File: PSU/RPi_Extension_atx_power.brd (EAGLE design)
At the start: 63 x 50 mm, 8 parts, among them J1 ATX24RH, J2 J2

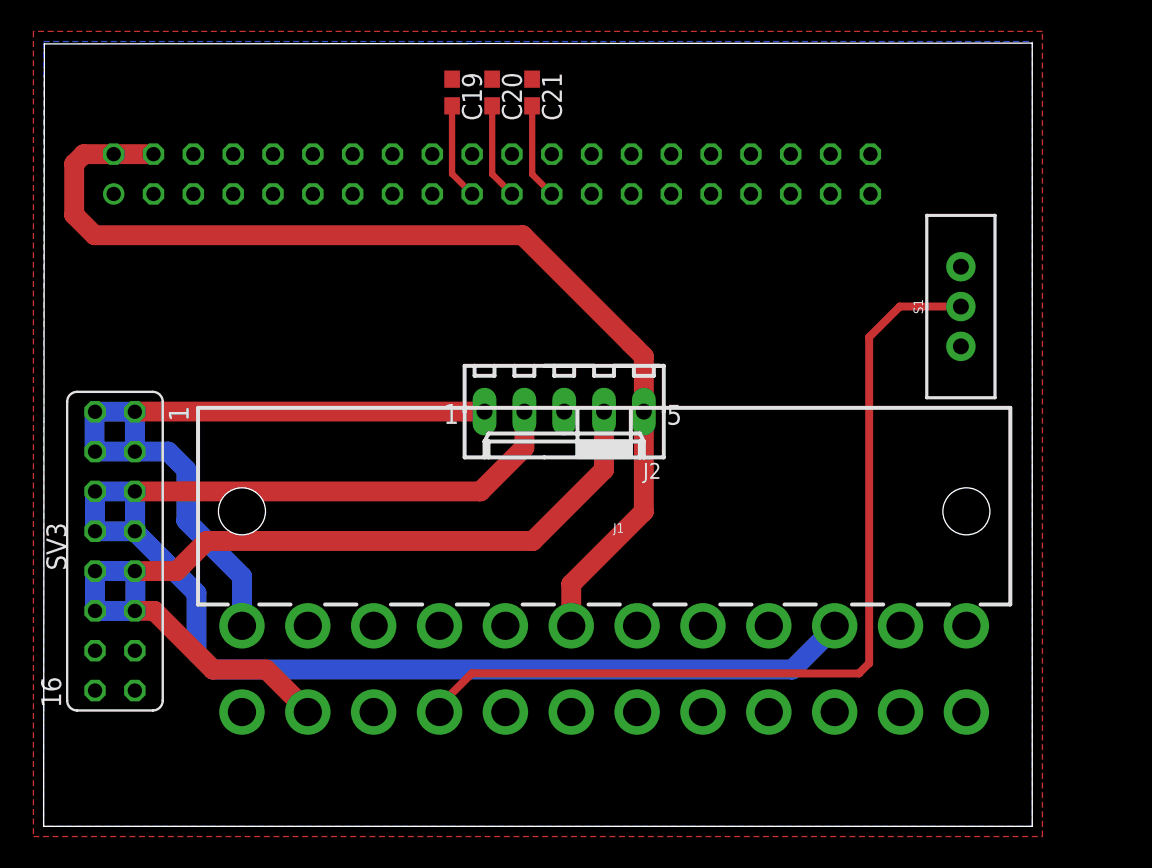
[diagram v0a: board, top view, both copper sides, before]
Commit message: added vertical connector to power board
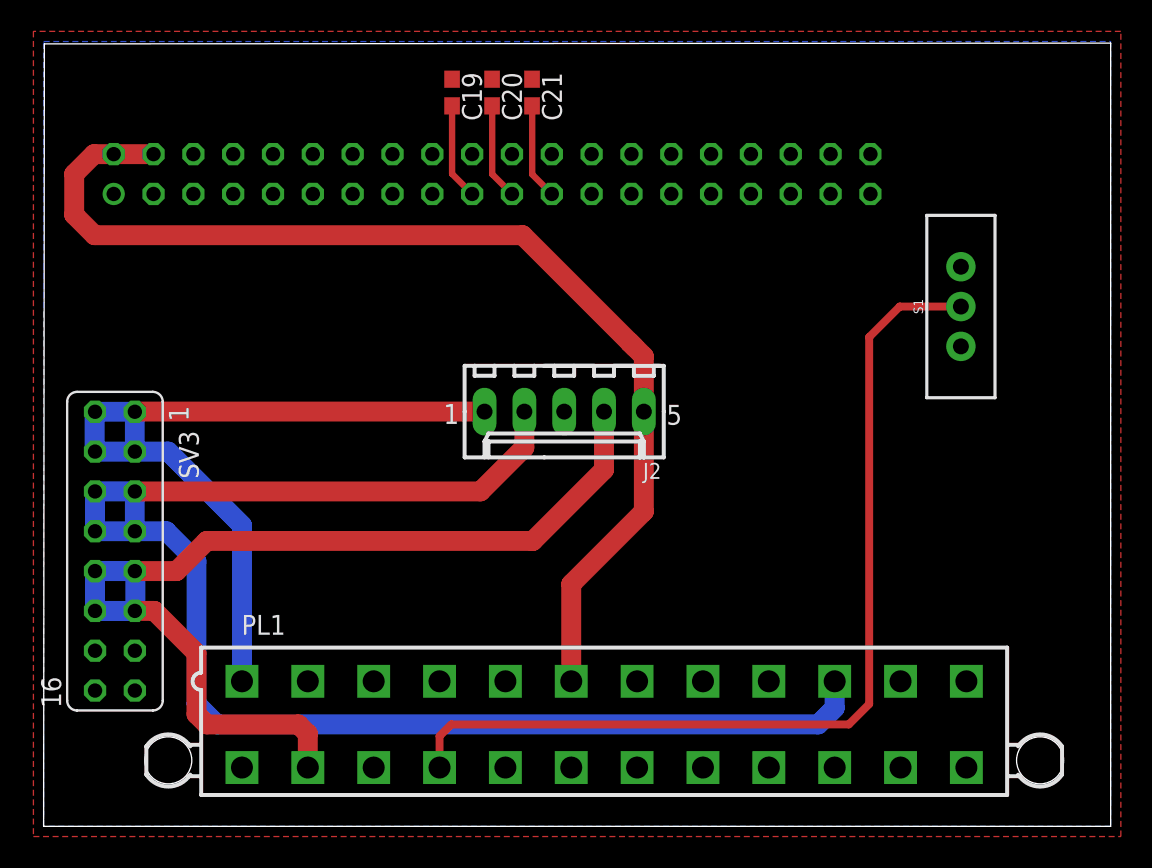
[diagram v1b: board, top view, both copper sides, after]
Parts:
- removed J1: ATX24RH, SparkFun-Connectors:ATX24_RIGHT_ANGLE
- added PL1: (no value), con-molex-2:5566-24
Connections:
- net +5V: now also PL1.6; no longer J1.6
- net DVCC: now also PL1.1; no longer J1.1
- net GND: now also PL1.15, PL1.17, PL1.18, PL1.19, PL1.24, PL1.3, PL1.5, PL1.7; no longer J1.15, J1.17, J1.18, J1.19, J1.24, J1.3, J1.5, J1.7
- net N$2: now also PL1.16; no longer J1.16
- net VDD: now also PL1.10; no longer J1.10
- net VSS: now also PL1.14; no longer J1.14
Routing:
- net VDD: track 90.2 -> 95.6 mm
- net VSS: track 60.3 -> 65.3 mm
- net N$2: track 56.4 -> 60.3 mm
- net DVCC: track 50.2 -> 53.7 mm
- net +5V: track 68.2 -> 71.4 mm
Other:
- board size 63 x 50 mm -> 68 x 50 mm
